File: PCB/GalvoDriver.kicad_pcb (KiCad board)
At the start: 4 copper layers, 56.5 x 61.7 mm, 33 parts, among them J1 Screw_Terminal_01x03, J2 Conn_01x03, J3 Conn_01x05_Male, J4 JUMPER_A, J5 JUMPER_B, J6 AudioJack3, J7 Conn_01x03, J8 Screw_Terminal_01x04, Q1 PN2222A, U1 TL082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

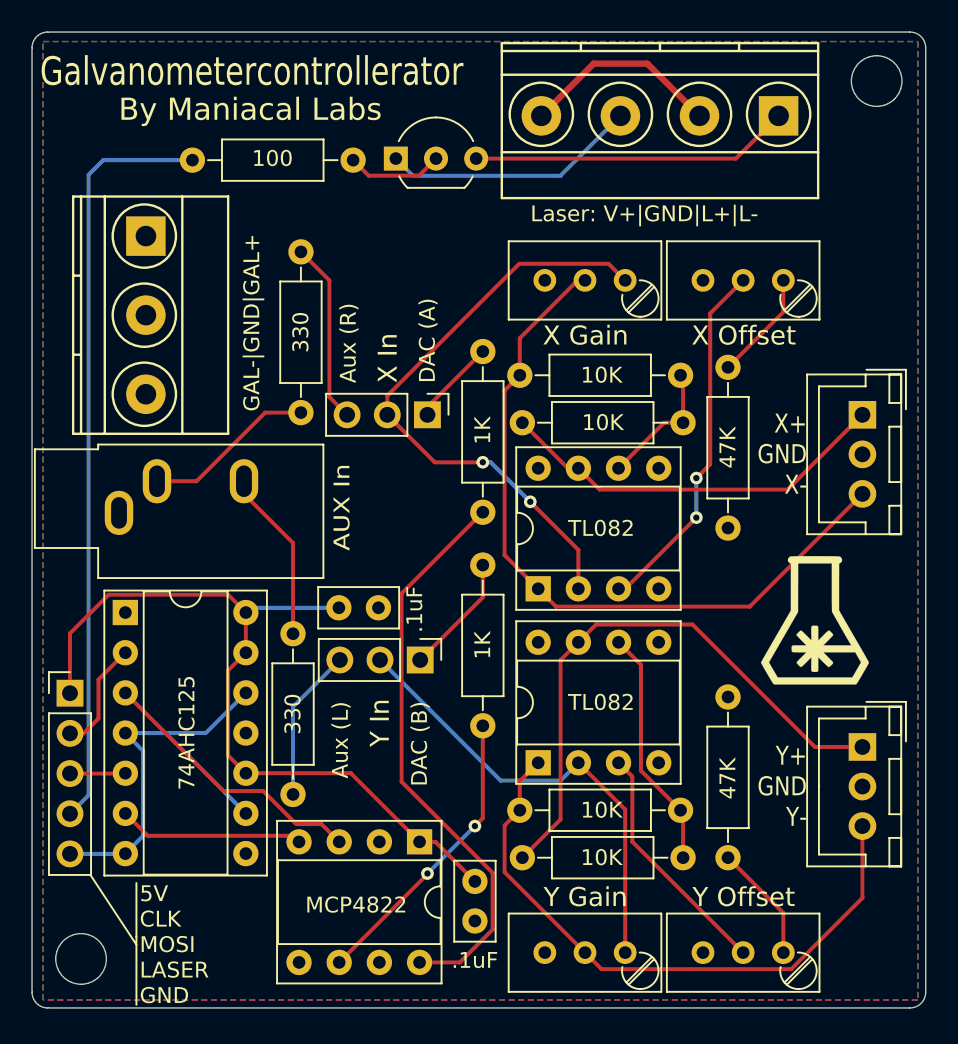
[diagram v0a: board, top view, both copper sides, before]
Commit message: Added CS connection to header, buffer, DAC input
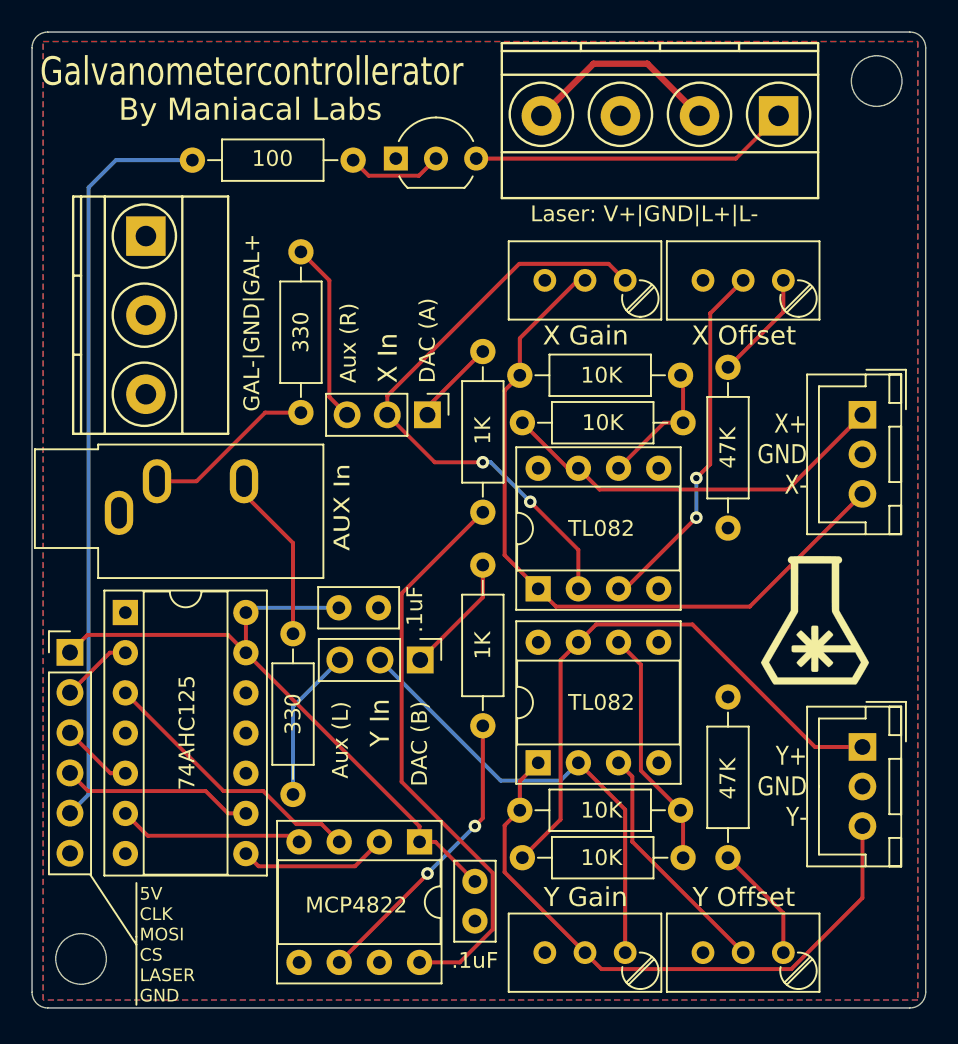
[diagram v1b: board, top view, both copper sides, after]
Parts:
- J3: value Conn_01x05_Male -> Conn_01x06_Male; footprint Pin_Headers:Pin_Header_Straight_1x05_Pitch2.54mm -> Pin_Headers:Pin_Header_Straight_1x06_Pitch2.54mm
- moved J3 2.58 mm to (35.4, 74.0)
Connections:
- J3 pad 4: LASER -> Net-(J3-Pad4)
- J3 pad 5: GND -> LASER
- U2 pad 2: GND -> CS
- U4 pad 10: VDD -> GND
- U4 pad 8: Net-(U4-Pad8) -> CS
- U4 pad 9: GND -> Net-(J3-Pad4)
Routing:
- net GND: track 46.7 -> 0.00 mm
- net Net-(J3-Pad4): track 0.00 -> 12.2 mm
- net CS: track 0.00 -> 9.41 mm
- net VDD: track 50.8 -> 41.6 mm
- net Net-(J3-Pad2): track 7.05 -> 4.54 mm
- net Net-(J3-Pad3): track 3.51 -> 4.56 mm
- net LASER: track 47.8 -> 47.3 mm
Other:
- board text added: "5V CLK MOSI CS LASER GND"
- board text removed: "5V CLK MOSI LASER GND"

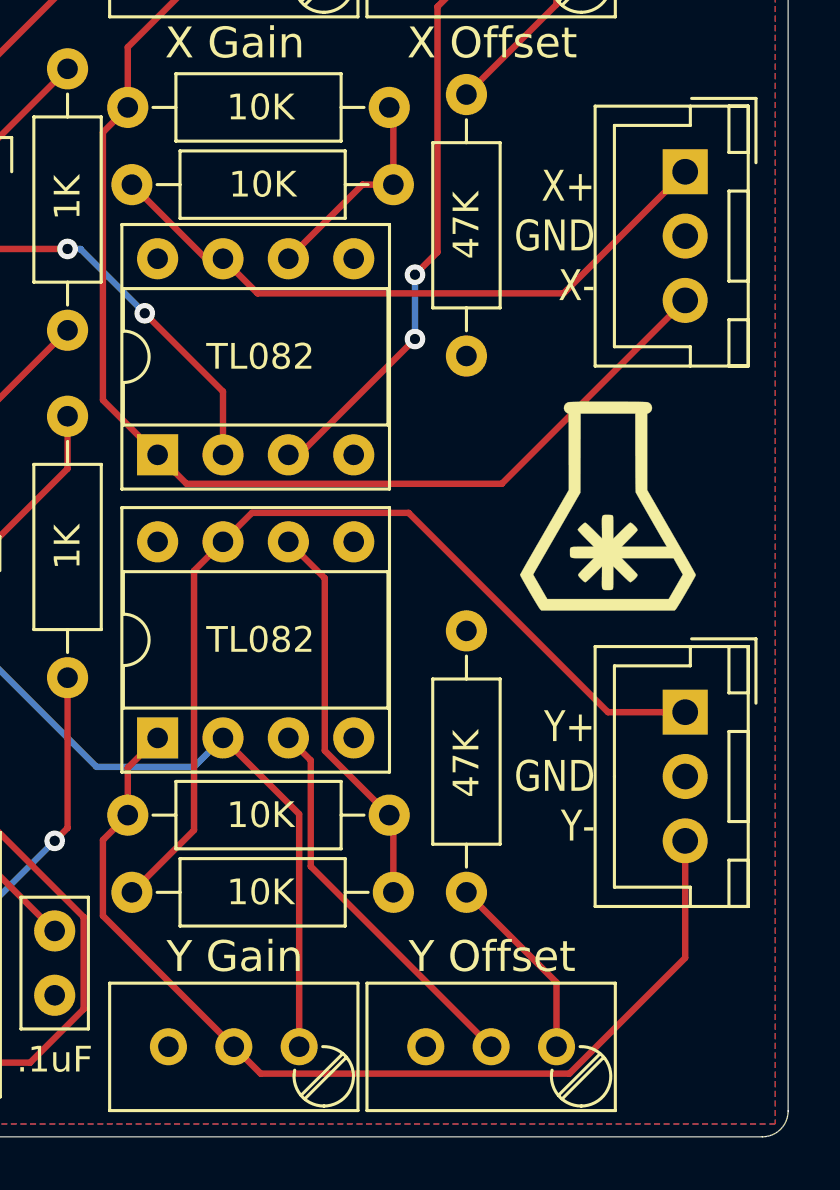
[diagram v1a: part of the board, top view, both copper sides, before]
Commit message: Flipped ILDA connector wiring and silkscreen labels
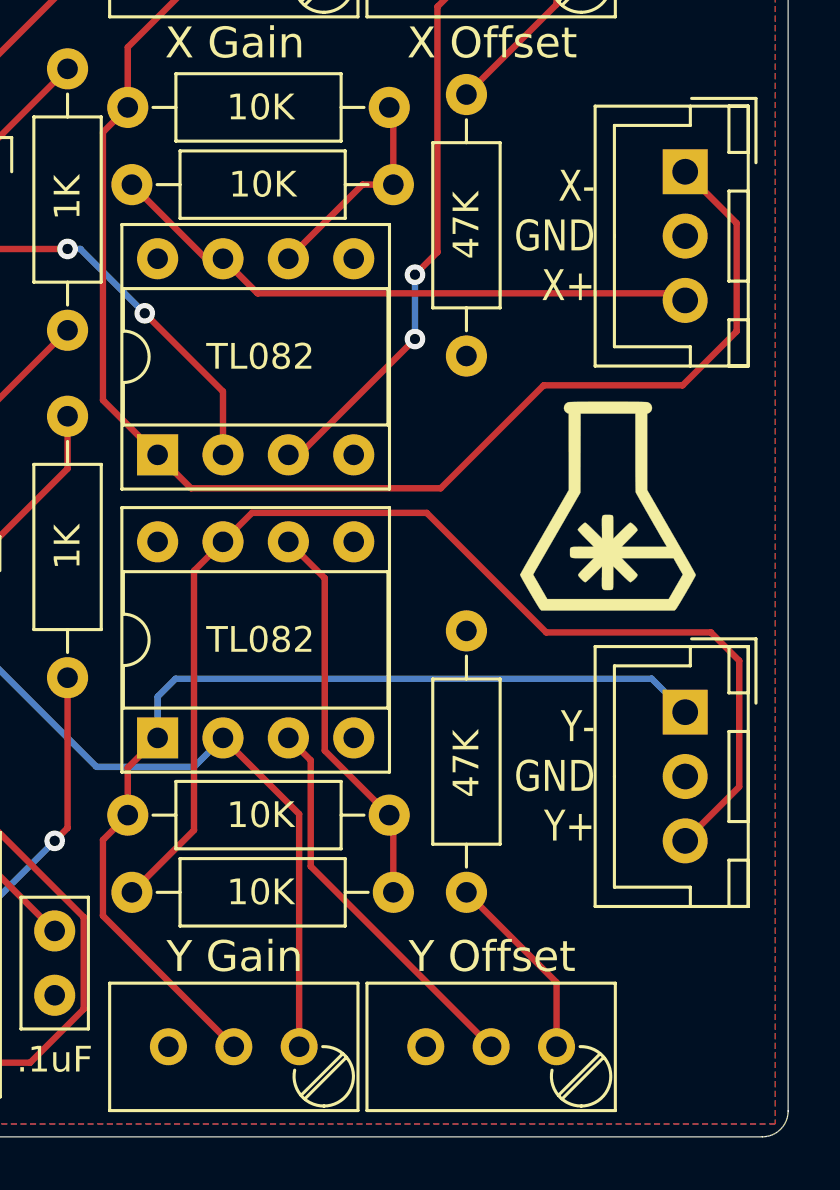
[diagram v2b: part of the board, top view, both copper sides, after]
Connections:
- J2 pad 1: A_ILDA+ -> A_ILDA-
- J2 pad 3: A_ILDA- -> A_ILDA+
- J7 pad 1: B_ILDA+ -> B_ILDA-
- J7 pad 3: B_ILDA- -> B_ILDA+
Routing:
- net B_ILDA+: track 36.7 -> 45.9 mm
- net A_ILDA-: track 46.7 -> 55.3 mm
- net A_ILDA+: track 25.2 -> 23.4 mm
- net B_ILDA-: track 39.4 -> 37.9 mm
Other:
- board text added: "X- GND X+"
- board text added: "Y- GND Y+"
- board text removed: "X+ GND X-"
- board text removed: "Y+ GND Y-"
